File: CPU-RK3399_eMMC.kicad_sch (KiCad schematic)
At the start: 1 part, among them U1 RK3399

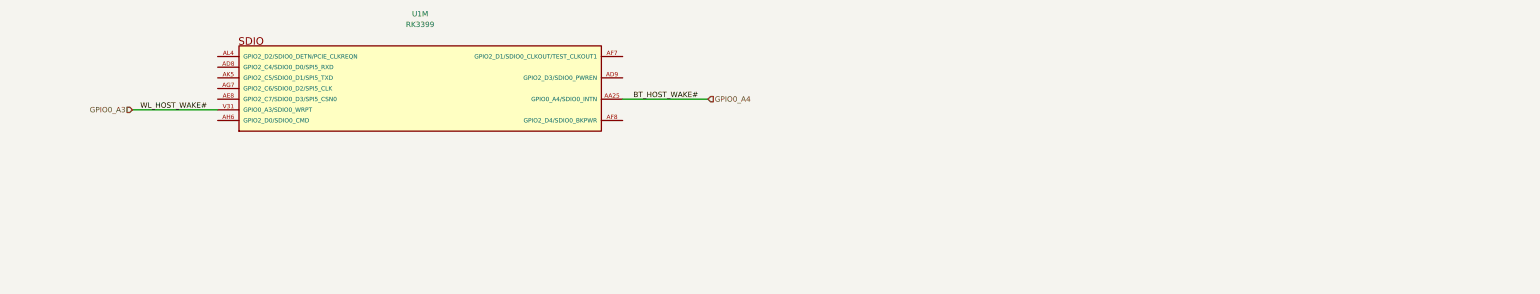
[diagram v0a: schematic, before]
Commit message: design CPU-RK3399 eMMC Controller
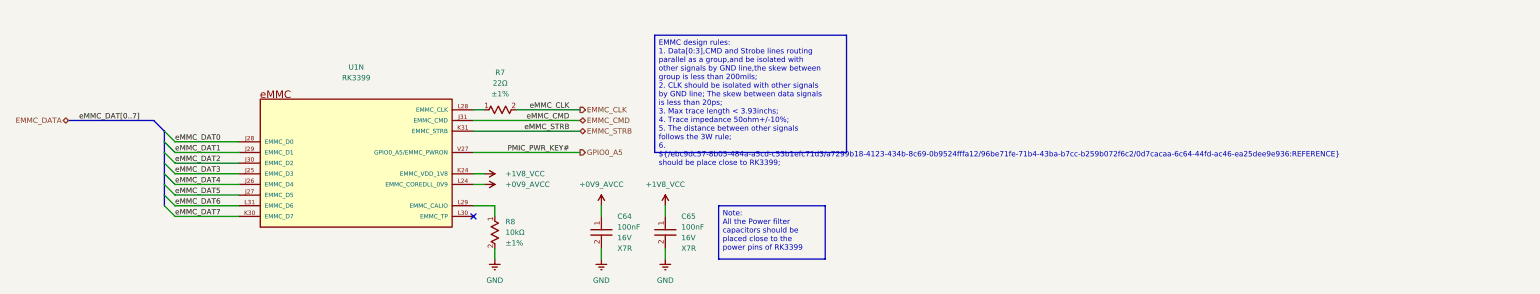
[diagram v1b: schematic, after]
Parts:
- removed U1: RK3399, footprints:BGA828C65P31X31_2100X2100X161, symbol component_library:System On Chip (SoC)/RK3399
- added C64, C65: ~, footprints:CAPC1005X50N, symbol component_library:Capacitors/CL05B104KO5NNNC
- added R7: ~, footprints:RESC1005X35N, symbol component_library:Resistors/0402WGF220JTCE
- added R8: ~, footprints:RESC1005X35N, symbol component_library:Resistors/0402WGF1002TCE
- added U1: RK3399, footprints:BGA828C65P31X31_2100X2100X161, symbol component_library:System On Chip (SoC)/RK3399
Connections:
- new net: R7.1, U1.L28 (EMMC_CLK)
- new net: R8.1, U1.L29 (EMMC_CALIO)
- new net +0V9_AVCC: C64.1, U1.L24 (EMMC_COREDLL_0V9)
- new net +1V8_VCC: C65.1, U1.K24 (EMMC_VDD_1V8)
- new net EMMC_CLK: R7.2
- new net EMMC_CMD: U1.J31 (EMMC_CMD)
- new net EMMC_STRB: U1.K31 (EMMC_STRB)
- new net GND: C64.2, C65.2, R8.2
- new net GPIO0_A5: U1.V27 (GPIO0_A5/EMMC_PWRON)
- new net eMMC_DAT0: U1.J28 (EMMC_D0)
- new net eMMC_DAT1: U1.J29 (EMMC_D1)
- new net eMMC_DAT2: U1.J30 (EMMC_D2)
- new net eMMC_DAT3: U1.J25 (EMMC_D3)
- new net eMMC_DAT4: U1.J26 (EMMC_D4)
- new net eMMC_DAT5: U1.J27 (EMMC_D5)
- new net eMMC_DAT6: U1.L31 (EMMC_D6)
- new net eMMC_DAT7: U1.K30 (EMMC_D7)
- no-connect marks 0 -> 1
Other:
- title: (none) -> CPU-RK3399 eMMC Controller

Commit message: update design power
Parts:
- renumbered C64 to C117, C65 to C118, R7 to R30, R8 to R31, U1 to U2
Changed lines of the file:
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@@
 		(on_board yes)
 		(dnp no)
-		(property "Reference" "#PWR041"
+		(property "Reference" "#PWR0122"
 			(at 193.04 115.57 0)
 			(effects
@@
 			(project "VESA-SBC3399"
 				(path "/ebc9dc57-8b05-484a-a5cd-c53b1efc71d3/a7299b18-4123-434b-8c69-0b9524fffa12/96be71fe-71b4-43ba-b7cc-b259b072f6c2"
-					(reference "#PWR041")
+					(reference "#PWR0122")
 					(unit 1)
 				)
@@
 		(dnp no)
 		(fields_autoplaced yes)
-		(property "Reference" "R7"
+		(property "Reference" "R30"
 			(at 168.91 80.01 0)
 			(effects
@@
 			(project "VESA-SBC3399"
 				(path "/ebc9dc57-8b05-484a-a5cd-c53b1efc71d3/a7299b18-4123-434b-8c69-0b9524fffa12/96be71fe-71b4-43ba-b7cc-b259b072f6c2"
-					(reference "R7")
+					(reference "R30")
 					(unit 1)
 				)
@@
 		(dnp no)
 		(fields_autoplaced yes)
-		(property "Reference" "U1"
+		(property "Reference" "U2"
 			(at 134.62 78.74 0)
 			(effects
@@
 			(project "VESA-SBC3399"
 				(path "/ebc9dc57-8b05-484a-a5cd-c53b1efc71d3/a7299b18-4123-434b-8c69-0b9524fffa12/96be71fe-71b4-43ba-b7cc-b259b072f6c2"
-					(reference "U1")
+					(reference "U2")
 					(unit 14)
 				)
@@
 		(dnp no)
 		(fields_autoplaced yes)
-		(property "Reference" "#PWR043"
+		(property "Reference" "#PWR0124"
 			(at 167.64 130.81 0)
 			(effects
@@
 			(project "VESA-SBC3399"
 				(path "/ebc9dc57-8b05-484a-a5cd-c53b1efc71d3/a7299b18-4123-434b-8c69-0b9524fffa12/96be71fe-71b4-43ba-b7cc-b259b072f6c2"
-					(reference "#PWR043")
+					(reference "#PWR0124")
 					(unit 1)
 				)
@@
 		(dnp no)
 		(fields_autoplaced yes)
-		(property "Reference" "#PWR044"
+		(property "Reference" "#PWR0125"
 			(at 193.04 130.81 0)
 			(effects
@@
 			(project "VESA-SBC3399"
 				(path "/ebc9dc57-8b05-484a-a5cd-c53b1efc71d3/a7299b18-4123-434b-8c69-0b9524fffa12/96be71fe-71b4-43ba-b7cc-b259b072f6c2"
-					(reference "#PWR044")
+					(reference "#PWR0125")
 					(unit 1)
 				)
@@
 		(on_board yes)
 		(dnp no)
-		(property "Reference" "#PWR040"
+		(property "Reference" "#PWR0121"
 			(at 161.29 106.68 0)
 			(effects
@@
 			(project "VESA-SBC3399"
 				(path "/ebc9dc57-8b05-484a-a5cd-c53b1efc71d3/a7299b18-4123-434b-8c69-0b9524fffa12/96be71fe-71b4-43ba-b7cc-b259b072f6c2"
-					(reference "#PWR040")
+					(reference "#PWR0121")
 					(unit 1)
 				)
@@
 		(dnp no)
 		(fields_autoplaced yes)
-		(property "Reference" "#PWR045"
+		(property "Reference" "#PWR0126"
 			(at 208.28 130.81 0)
 			(effects
@@
 			(project "VESA-SBC3399"
 				(path "/ebc9dc57-8b05-484a-a5cd-c53b1efc71d3/a7299b18-4123-434b-8c69-0b9524fffa12/96be71fe-71b4-43ba-b7cc-b259b072f6c2"
-					(reference "#PWR045")
+					(reference "#PWR0126")
 					(unit 1)
 				)
@@
 		(on_board yes)
 		(dnp no)
-		(property "Reference" "C65"
+		(property "Reference" "C118"
 			(at 212.09 114.2999 0)
 			(effects
@@
 			(project "VESA-SBC3399"
 				(path "/ebc9dc57-8b05-484a-a5cd-c53b1efc71d3/a7299b18-4123-434b-8c69-0b9524fffa12/96be71fe-71b4-43ba-b7cc-b259b072f6c2"
-					(reference "C65")
+					(reference "C118")
 					(unit 1)
 				)
@@
 		(on_board yes)
 		(dnp no)
-		(property "Reference" "#PWR039"
+		(property "Reference" "#PWR0120"
 			(at 161.29 104.14 0)
 			(effects
@@
 			(project "VESA-SBC3399"
 				(path "/ebc9dc57-8b05-484a-a5cd-c53b1efc71d3/a7299b18-4123-434b-8c69-0b9524fffa12/96be71fe-71b4-43ba-b7cc-b259b072f6c2"
-					(reference "#PWR039")
+					(reference "#PWR0120")
 					(unit 1)
 				)
@@
 		(dnp no)
 		(fields_autoplaced yes)
-		(property "Reference" "R8"
+		(property "Reference" "R31"
 			(at 170.18 115.5699 90)
 			(effects
@@
 			(project "VESA-SBC3399"
 				(path "/ebc9dc57-8b05-484a-a5cd-c53b1efc71d3/a7299b18-4123-434b-8c69-0b9524fffa12/96be71fe-71b4-43ba-b7cc-b259b072f6c2"
-					(reference "R8")
+					(reference "R31")
 					(unit 1)
 				)
@@
 		(on_board yes)
 		(dnp no)
-		(property "Reference" "C64"
+		(property "Reference" "C117"
 			(at 196.85 114.2999 0)
 			(effects
@@
 			(project "VESA-SBC3399"
 				(path "/ebc9dc57-8b05-484a-a5cd-c53b1efc71d3/a7299b18-4123-434b-8c69-0b9524fffa12/96be71fe-71b4-43ba-b7cc-b259b072f6c2"
-					(reference "C64")
+					(reference "C117")
 					(unit 1)
 				)
@@
 		(on_board yes)
 		(dnp no)
-		(property "Reference" "#PWR042"
+		(property "Reference" "#PWR0123"
 			(at 208.28 115.57 0)
 			(effects
@@
 			(project "VESA-SBC3399"
 				(path "/ebc9dc57-8b05-484a-a5cd-c53b1efc71d3/a7299b18-4123-434b-8c69-0b9524fffa12/96be71fe-71b4-43ba-b7cc-b259b072f6c2"
-					(reference "#PWR042")
+					(reference "#PWR0123")
 					(unit 1)
 				)

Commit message: design DDR
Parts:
- renumbered C117 to C244, C118 to C245, R30 to R101, R31 to R102, U2 to U17
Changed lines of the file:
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@@
 		(on_board yes)
 		(dnp no)
-		(property "Reference" "#PWR0122"
+		(property "Reference" "#PWR0282"
 			(at 193.04 115.57 0)
 			(effects
@@
 			(project "VESA-SBC3399"
 				(path "/ebc9dc57-8b05-484a-a5cd-c53b1efc71d3/a7299b18-4123-434b-8c69-0b9524fffa12/96be71fe-71b4-43ba-b7cc-b259b072f6c2"
-					(reference "#PWR0122")
+					(reference "#PWR0282")
 					(unit 1)
 				)
@@
 		(dnp no)
 		(fields_autoplaced yes)
-		(property "Reference" "R30"
+		(property "Reference" "R101"
 			(at 168.91 80.01 0)
 			(effects
@@
 			(project "VESA-SBC3399"
 				(path "/ebc9dc57-8b05-484a-a5cd-c53b1efc71d3/a7299b18-4123-434b-8c69-0b9524fffa12/96be71fe-71b4-43ba-b7cc-b259b072f6c2"
-					(reference "R30")
+					(reference "R101")
 					(unit 1)
 				)
@@
 		(dnp no)
 		(fields_autoplaced yes)
-		(property "Reference" "U2"
+		(property "Reference" "U17"
 			(at 134.62 78.74 0)
 			(effects
@@
 		)
 		(property "Footprint" "footprints:BGA828C65P31X31_2100X2100X161"
-			(at 152.4 106.68 0)
+			(at 134.62 106.68 0)
 			(effects
 				(font
@@
 			(project "VESA-SBC3399"
 				(path "/ebc9dc57-8b05-484a-a5cd-c53b1efc71d3/a7299b18-4123-434b-8c69-0b9524fffa12/96be71fe-71b4-43ba-b7cc-b259b072f6c2"
-					(reference "U2")
+					(reference "U17")
 					(unit 14)
 				)
@@
 		(dnp no)
 		(fields_autoplaced yes)
-		(property "Reference" "#PWR0124"
+		(property "Reference" "#PWR0284"
 			(at 167.64 130.81 0)
 			(effects
@@
 			(project "VESA-SBC3399"
 				(path "/ebc9dc57-8b05-484a-a5cd-c53b1efc71d3/a7299b18-4123-434b-8c69-0b9524fffa12/96be71fe-71b4-43ba-b7cc-b259b072f6c2"
-					(reference "#PWR0124")
+					(reference "#PWR0284")
 					(unit 1)
 				)
@@
 		(dnp no)
 		(fields_autoplaced yes)
-		(property "Reference" "#PWR0125"
+		(property "Reference" "#PWR0285"
 			(at 193.04 130.81 0)
 			(effects
@@
 			(project "VESA-SBC3399"
 				(path "/ebc9dc57-8b05-484a-a5cd-c53b1efc71d3/a7299b18-4123-434b-8c69-0b9524fffa12/96be71fe-71b4-43ba-b7cc-b259b072f6c2"
-					(reference "#PWR0125")
+					(reference "#PWR0285")
 					(unit 1)
 				)
@@
 		(on_board yes)
 		(dnp no)
-		(property "Reference" "#PWR0121"
+		(property "Reference" "#PWR0281"
 			(at 161.29 106.68 0)
 			(effects
@@
 			(project "VESA-SBC3399"
 				(path "/ebc9dc57-8b05-484a-a5cd-c53b1efc71d3/a7299b18-4123-434b-8c69-0b9524fffa12/96be71fe-71b4-43ba-b7cc-b259b072f6c2"
-					(reference "#PWR0121")
+					(reference "#PWR0281")
 					(unit 1)
 				)
@@
 		(dnp no)
 		(fields_autoplaced yes)
-		(property "Reference" "#PWR0126"
+		(property "Reference" "#PWR0286"
 			(at 208.28 130.81 0)
 			(effects
@@
 			(project "VESA-SBC3399"
 				(path "/ebc9dc57-8b05-484a-a5cd-c53b1efc71d3/a7299b18-4123-434b-8c69-0b9524fffa12/96be71fe-71b4-43ba-b7cc-b259b072f6c2"
-					(reference "#PWR0126")
+					(reference "#PWR0286")
 					(unit 1)
 				)
@@
 		(on_board yes)
 		(dnp no)
-		(property "Reference" "C118"
+		(property "Reference" "C245"
 			(at 212.09 114.2999 0)
 			(effects
@@
 			(project "VESA-SBC3399"
 				(path "/ebc9dc57-8b05-484a-a5cd-c53b1efc71d3/a7299b18-4123-434b-8c69-0b9524fffa12/96be71fe-71b4-43ba-b7cc-b259b072f6c2"
-					(reference "C118")
+					(reference "C245")
 					(unit 1)
 				)
@@
 		(on_board yes)
 		(dnp no)
-		(property "Reference" "#PWR0120"
+		(property "Reference" "#PWR0280"
 			(at 161.29 104.14 0)
 			(effects
@@
 			(project "VESA-SBC3399"
 				(path "/ebc9dc57-8b05-484a-a5cd-c53b1efc71d3/a7299b18-4123-434b-8c69-0b9524fffa12/96be71fe-71b4-43ba-b7cc-b259b072f6c2"
-					(reference "#PWR0120")
+					(reference "#PWR0280")
 					(unit 1)
 				)
@@
 		(dnp no)
 		(fields_autoplaced yes)
-		(property "Reference" "R31"
+		(property "Reference" "R102"
 			(at 170.18 115.5699 90)
 			(effects
@@
 			(project "VESA-SBC3399"
 				(path "/ebc9dc57-8b05-484a-a5cd-c53b1efc71d3/a7299b18-4123-434b-8c69-0b9524fffa12/96be71fe-71b4-43ba-b7cc-b259b072f6c2"
-					(reference "R31")
+					(reference "R102")
 					(unit 1)
 				)
@@
 		(on_board yes)
 		(dnp no)
-		(property "Reference" "C117"
+		(property "Reference" "C244"
 			(at 196.85 114.2999 0)
 			(effects
@@
 			(project "VESA-SBC3399"
 				(path "/ebc9dc57-8b05-484a-a5cd-c53b1efc71d3/a7299b18-4123-434b-8c69-0b9524fffa12/96be71fe-71b4-43ba-b7cc-b259b072f6c2"
-					(reference "C117")
+					(reference "C244")
 					(unit 1)
 				)
@@
 		(on_board yes)
 		(dnp no)
-		(property "Reference" "#PWR0123"
+		(property "Reference" "#PWR0283"
 			(at 208.28 115.57 0)
 			(effects
@@
 			(project "VESA-SBC3399"
 				(path "/ebc9dc57-8b05-484a-a5cd-c53b1efc71d3/a7299b18-4123-434b-8c69-0b9524fffa12/96be71fe-71b4-43ba-b7cc-b259b072f6c2"
-					(reference "#PWR0123")
+					(reference "#PWR0283")
 					(unit 1)
 				)
